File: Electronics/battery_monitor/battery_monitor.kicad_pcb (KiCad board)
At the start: 2 copper layers, 43 x 19.8 mm, 23 parts, among them IC1 MIC2779H-1YM5_TR, J1 Conn_01x04_Male, J2 Conn_01x02_Pin, J3 Conn_01x02_Pin, Q2 DMP4015SK3-13, Q4 BSS123LT1G, U1 MCP1700x-120xxMB, U2 INA226

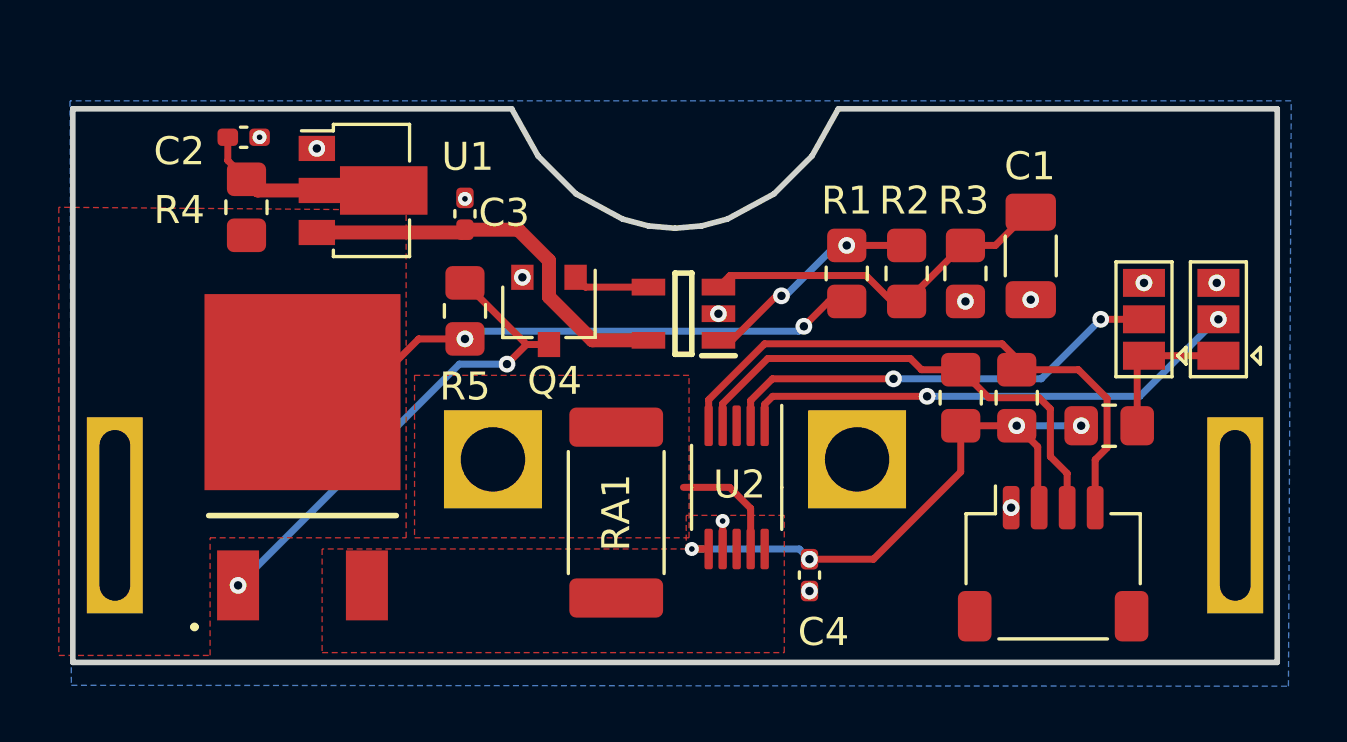
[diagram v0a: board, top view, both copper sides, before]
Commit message: Add main robot PCB
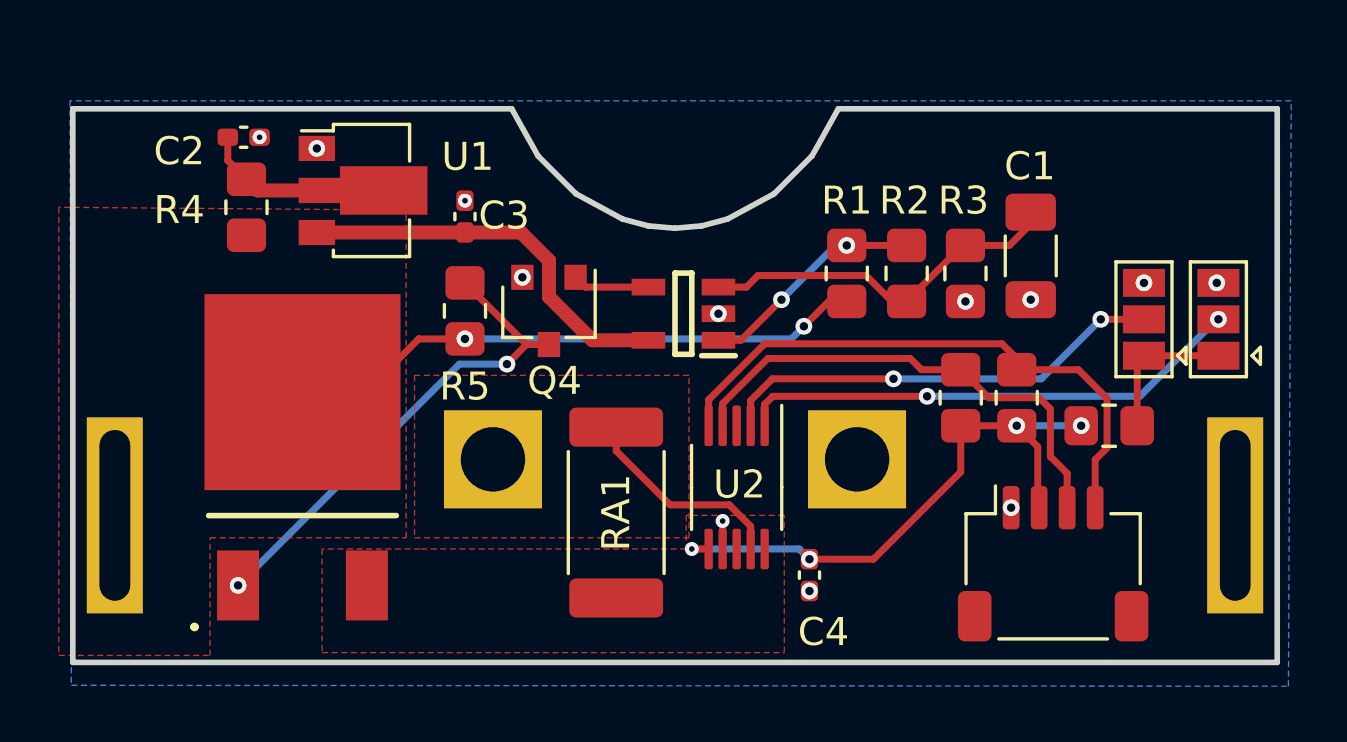
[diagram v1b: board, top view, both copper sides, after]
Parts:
- R1: value 920k -> 920k 1%
- moved C3 0.10 mm to (54.4, 25.2)
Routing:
- net Net-(J3-Pin_1): track 4.16 -> 7.58 mm

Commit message: Add missing GameState file
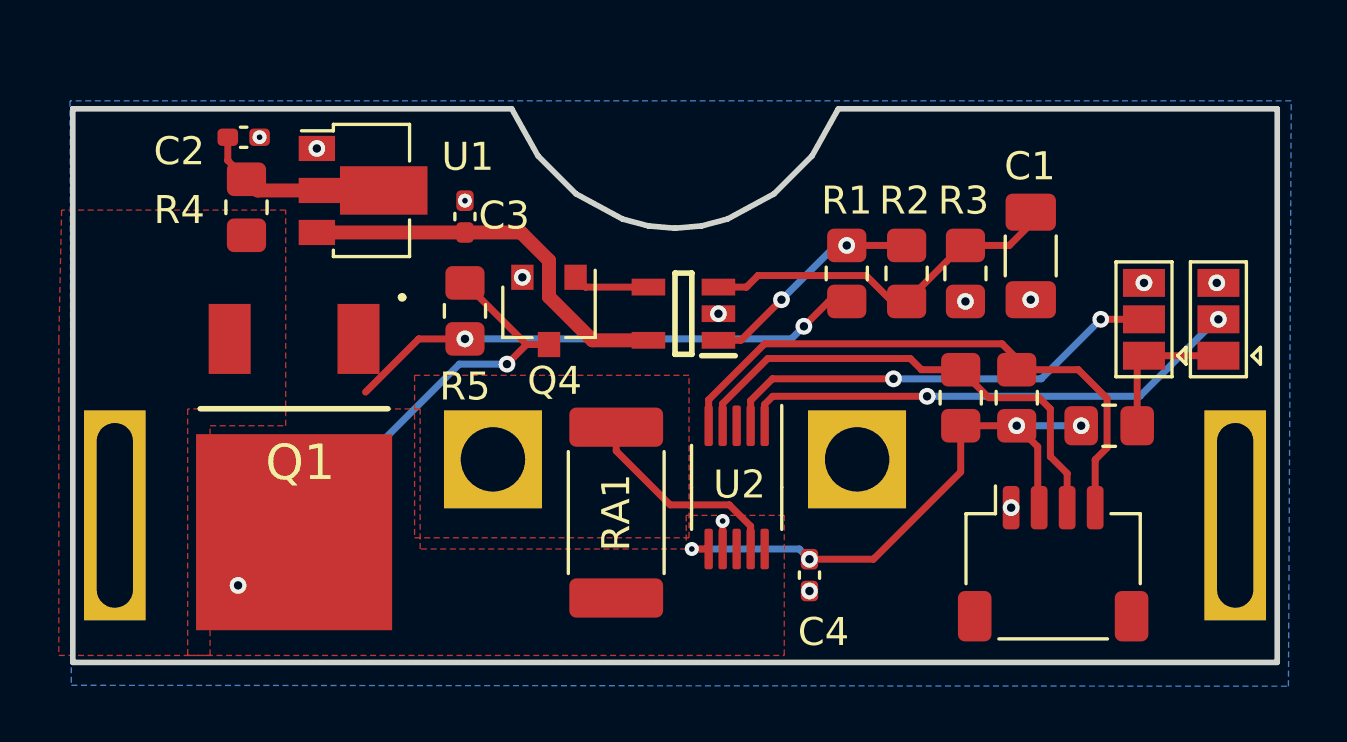
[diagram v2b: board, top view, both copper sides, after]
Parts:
- removed Q2: DMP4015SK3-13, MIC2779L-1YM5_TR:AZ1084CD50TRG1
- added Q1: DMP4015SK3-13, MIC2779L-1YM5_TR:AZ1084CD50TRG1, F.Cu at (48.3, 32.1)
- Q4: value BSS123LT1G -> BS170
- U1: value MCP1700x-120xxMB -> HT7533; LDI8233-05U

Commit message: Electronics: correction to battery_monitor PCB
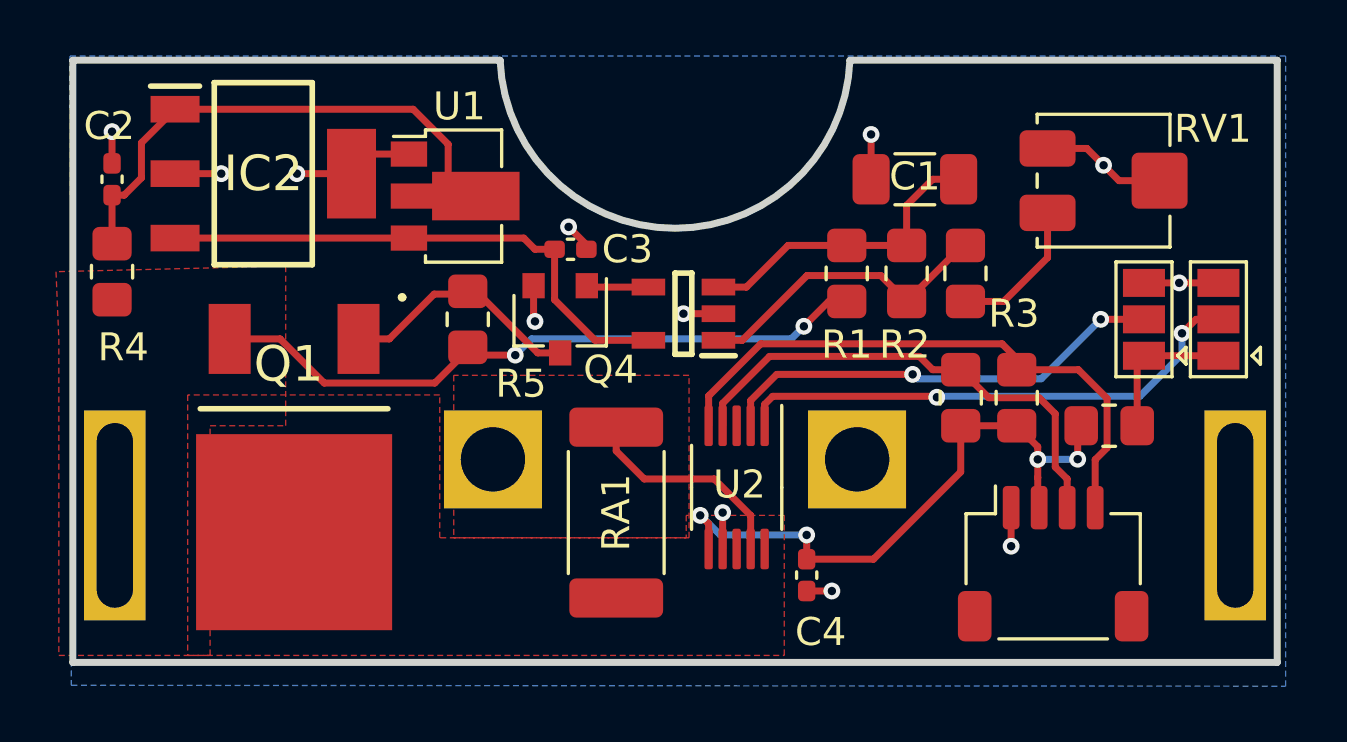
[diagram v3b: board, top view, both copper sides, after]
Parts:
- added IC2: MCP1790-3302E_DB, MCP1790-3302E_DB:SOT230P700X180-4N, F.Cu at (47.2, 23.7)
- added RV1: 20k, Potentiometer_SMD:Potentiometer_Bourns_3314J_Vertical, F.Cu at (77.2, 23.9)
- R3: value 75k 1% -> 65k
- moved R4 5.32 mm to (41.8, 27.2)
- moved C1 4.96 mm to (70.5, 23.9), turned to 180 degrees
- moved C2 4.93 mm to (41.8, 23.9), turned to -90 degrees
- moved C3 3.94 mm to (58.2, 26.4), turned to 180 degrees
- moved U1 3.29 mm to (54.4, 24.5)
- moved Q4 0.50 mm to (57.8, 28.9)
- moved R5 0.32 mm to (54.5, 28.9)
- moved C4 0.10 mm to (66.6, 38.0)
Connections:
- R1 pad 2: Net-(IC1-HTH) -> Net-(IC1-LTH)
- R2 pad 1: Net-(IC1-HTH) -> Net-(IC1-LTH)
- R2 pad 2: Net-(IC1-LTH) -> Net-(IC1-HTH)
- R3 pad 1: Net-(IC1-LTH) -> Net-(IC1-HTH)
- R3 pad 2: GND -> Net-(R3-Pad2)
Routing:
- net GND: track 1.00 -> 23.0 mm
- net Net-(IC2-VIN): track 4.54 -> 19.4 mm
- net Net-(Q1-G): track 17.8 -> 8.73 mm, vias 2 -> 0
- net +BATT: track 18.5 -> 23.9 mm
- net Net-(R3-Pad2): track 0.00 -> 5.28 mm
- net VDD: track 14.2 -> 19.5 mm
- net Net-(IC1-HTH): track 8.34 -> 10.9 mm, vias 2 -> 0
- net +3.3V: track 20.8 -> 22.6 mm
- net Net-(IC1-LTH): track 12.2 -> 11.0 mm
- net Net-(IC1-~{RST}): track 2.74 -> 2.20 mm
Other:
- board size 43 x 19.8 mm -> 43 x 21.5 mm
